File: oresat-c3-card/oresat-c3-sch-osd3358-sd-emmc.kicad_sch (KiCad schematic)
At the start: 48 parts, among them J5 DM3BT-DSF-PEJS, U1 OSD3358-1G-ISM, U8 TCAN330, U9 SFEM016GB1EA1TO-I-GE-121-STD

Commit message: All footprints updated. Passes ERC/DRC.
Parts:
- C16, C25: footprint Capacitor_SMD:C_0805_2012Metric -> oresat-passives:0805-C-NOSILK; DPN 490-GRT21BC71E106KE13LCT-ND -> 490-GRT21BC71E106KE13KCT-ND; DST Digi-Key -> DigiKey; MPN GRT21BC71E106KE13L -> GRT21BC71E106KE13K
- C17, C18: footprint Capacitor_SMD:C_0603_1608Metric -> oresat-passives:0603-C-NOSILK; DPN 587-3472-1-ND -> 399-6856-1-ND; MFR Taiyo Yuden -> KEMET; MPN TMK107BJ104KAHT -> C0603C104K5RACAUTO
- C19, C20, C21, C22, C23, C24: footprint Capacitor_SMD:C_0603_1608Metric -> oresat-passives:0603-C-NOSILK; DPN 587-3473-1-ND -> 490-GRT188R71E105KE13DCT-ND; MFR Taiyo Yuden -> Murata Electronics; MPN TMK107BJ105KAHT -> GRT188R71E105KE13D
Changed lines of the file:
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@@
 			)
 		)
-		(property "Footprint" "Capacitor_SMD:C_0603_1608Metric"
+		(property "Footprint" "oresat-passives:0603-C-NOSILK"
 			(at 360.68 149.86 0)
 			(effects
@@
 			)
 		)
-		(property "Datasheet" "~"
+		(property "Datasheet" "https://search.murata.co.jp/Ceramy/image/img/A01X/G101/ENG/GRT188R71E105KE13-01.pdf"
 			(at 360.68 149.86 0)
 			(effects
@@
 			)
 		)
-		(property "Description" "1µF ±10% 25V Ceramic Capacitor X5R 0603 (1608 Metric)"
+		(property "Description" "1 µF ±10% 25V Ceramic Capacitor X7R 0603 (1608 Metric)"
 			(at 360.68 149.86 0)
 			(effects
@@
 			)
 		)
-		(property "DPN" "587-3473-1-ND"
+		(property "DPN" "490-GRT188R71E105KE13DCT-ND"
 			(at 360.68 149.86 0)
 			(effects
@@
 			)
 		)
-		(property "MFR" "Taiyo Yuden"
+		(property "MFR" "Murata Electronics"
 			(at 360.68 149.86 0)
 			(effects
@@
 			)
 		)
-		(property "MPN" "TMK107BJ105KAHT"
+		(property "MPN" "GRT188R71E105KE13D"
 			(at 360.68 149.86 0)
 			(effects
@@
 			)
 		)
-		(property "Footprint" "Capacitor_SMD:C_0603_1608Metric"
+		(property "Footprint" "oresat-passives:0603-C-NOSILK"
 			(at 383.54 149.86 0)
 			(effects
@@
 			)
 		)
-		(property "Datasheet" "~"
+		(property "Datasheet" "https://search.murata.co.jp/Ceramy/image/img/A01X/G101/ENG/GRT188R71E105KE13-01.pdf"
 			(at 383.54 149.86 0)
 			(effects
@@
 			)
 		)
-		(property "Description" "1µF ±10% 25V Ceramic Capacitor X5R 0603 (1608 Metric)"
+		(property "Description" "1 µF ±10% 25V Ceramic Capacitor X7R 0603 (1608 Metric)"
 			(at 383.54 149.86 0)
 			(effects
@@
 			)
 		)
-		(property "DPN" "587-3473-1-ND"
+		(property "DPN" "490-GRT188R71E105KE13DCT-ND"
 			(at 383.54 149.86 0)
 			(effects
@@
 			)
 		)
-		(property "MFR" "Taiyo Yuden"
+		(property "MFR" "Murata Electronics"
 			(at 383.54 149.86 0)
 			(effects
@@
 			)
 		)
-		(property "MPN" "TMK107BJ105KAHT"
+		(property "MPN" "GRT188R71E105KE13D"
 			(at 383.54 149.86 0)
 			(effects
@@
 			)
 		)
-		(property "Footprint" "Capacitor_SMD:C_0805_2012Metric"
+		(property "Footprint" "oresat-passives:0805-C-NOSILK"
 			(at 57.15 110.49 0)
 			(effects
@@
 			)
 		)
-		(property "Datasheet" "~"
+		(property "Datasheet" "https://search.murata.co.jp/Ceramy/image/img/A01X/G101/ENG/GRT21BC71E106KE13-01.pdf"
 			(at 57.15 110.49 0)
 			(effects
@@
 			)
 		)
-		(property "DPN" "490-GRT21BC71E106KE13LCT-ND"
+		(property "DPN" "490-GRT21BC71E106KE13KCT-ND"
 			(at 57.15 110.49 0)
 			(effects
@@
 			)
 		)
-		(property "DST" "Digi-Key"
+		(property "DST" "DigiKey"
 			(at 57.15 110.49 0)
 			(effects
@@
 			)
 		)
-		(property "MPN" "GRT21BC71E106KE13L"
+		(property "MPN" "GRT21BC71E106KE13K"
 			(at 57.15 110.49 0)
 			(effects
@@
 			)
 		)
-		(property "Footprint" "Capacitor_SMD:C_0603_1608Metric"
+		(property "Footprint" "oresat-passives:0603-C-NOSILK"
 			(at 368.3 149.86 0)
 			(effects
@@
 			)
 		)
-		(property "Datasheet" "~"
+		(property "Datasheet" "https://search.murata.co.jp/Ceramy/image/img/A01X/G101/ENG/GRT188R71E105KE13-01.pdf"
 			(at 368.3 149.86 0)
 			(effects
@@
 			)
 		)
-		(property "Description" "1µF ±10% 25V Ceramic Capacitor X5R 0603 (1608 Metric)"
+		(property "Description" "1 µF ±10% 25V Ceramic Capacitor X7R 0603 (1608 Metric)"
 			(at 368.3 149.86 0)
 			(effects
@@
 			)
 		)
-		(property "DPN" "587-3473-1-ND"
+		(property "DPN" "490-GRT188R71E105KE13DCT-ND"
 			(at 368.3 149.86 0)
 			(effects
@@
 			)
 		)
-		(property "MFR" "Taiyo Yuden"
+		(property "MFR" "Murata Electronics"
 			(at 368.3 149.86 0)
 			(effects
@@
 			)
 		)
-		(property "MPN" "TMK107BJ105KAHT"
+		(property "MPN" "GRT188R71E105KE13D"
 			(at 368.3 149.86 0)
 			(effects
@@
 			)
 		)
-		(property "Footprint" "Capacitor_SMD:C_0603_1608Metric"
+		(property "Footprint" "oresat-passives:0603-C-NOSILK"
 			(at 345.44 149.86 0)
 			(effects
@@
 			)
 		)
-		(property "Datasheet" "~"
+		(property "Datasheet" "https://search.murata.co.jp/Ceramy/image/img/A01X/G101/ENG/GRT188R71E105KE13-01.pdf"
 			(at 345.44 149.86 0)
 			(effects
@@
 			)
 		)
-		(property "Description" "1µF ±10% 25V Ceramic Capacitor X5R 0603 (1608 Metric)"
+		(property "Description" "1 µF ±10% 25V Ceramic Capacitor X7R 0603 (1608 Metric)"
 			(at 345.44 149.86 0)
 			(effects
@@
 			)
 		)
-		(property "DPN" "587-3473-1-ND"
+		(property "DPN" "490-GRT188R71E105KE13DCT-ND"
 			(at 345.44 149.86 0)
 			(effects
@@
 			)
 		)
-		(property "MFR" "Taiyo Yuden"
+		(property "MFR" "Murata Electronics"
 			(at 345.44 149.86 0)
 			(effects
@@
 			)
 		)
-		(property "MPN" "TMK107BJ105KAHT"
+		(property "MPN" "GRT188R71E105KE13D"
 			(at 345.44 149.86 0)
 			(effects
@@
 			)
 		)
-		(property "Footprint" "Capacitor_SMD:C_0603_1608Metric"
+		(property "Footprint" "oresat-passives:0603-C-NOSILK"
 			(at 176.53 48.26 0)
 			(effects
@@
 			)
 		)
-		(property "Datasheet" "~"
+		(property "Datasheet" "https://search.kemet.com/download/specsheet/C0603C104K5RACAUTO"
 			(at 176.53 48.26 0)
 			(effects
@@
 			)
 		)
-		(property "Description" "100 nF (0.1µF) ±10% 25V Ceramic Capacitor X5R 0603 (1608 Metric)"
+		(property "Description" "0.1 µF ±10% 50V Ceramic Capacitor X7R 0603 (1608 Metric)"
 			(at 176.53 48.26 0)
 			(effects
@@
 			)
 		)
-		(property "DPN" "587-3472-1-ND"
+		(property "DPN" "399-6856-1-ND"
 			(at 176.53 48.26 0)
 			(effects
@@
 			)
 		)
-		(property "MFR" "Taiyo Yuden"
+		(property "MFR" "KEMET"
 			(at 176.53 48.26 0)
 			(effects
@@
 			)
 		)
-		(property "MPN" "TMK107BJ104KAHT"
+		(property "MPN" "C0603C104K5RACAUTO"
 			(at 176.53 48.26 0)
 			(effects
@@
 			)
 		)
-		(property "Footprint" "Capacitor_SMD:C_0603_1608Metric"
+		(property "Footprint" "oresat-passives:0603-C-NOSILK"
 			(at 375.92 149.86 0)
 			(effects
@@
 			)
 		)
-		(property "Datasheet" "~"
+		(property "Datasheet" "https://search.murata.co.jp/Ceramy/image/img/A01X/G101/ENG/GRT188R71E105KE13-01.pdf"
 			(at 375.92 149.86 0)
 			(effects
@@
 			)
 		)
-		(property "Description" "1µF ±10% 25V Ceramic Capacitor X5R 0603 (1608 Metric)"
+		(property "Description" "1 µF ±10% 25V Ceramic Capacitor X7R 0603 (1608 Metric)"
 			(at 375.92 149.86 0)
 			(effects
@@
 			)
 		)
-		(property "DPN" "587-3473-1-ND"
+		(property "DPN" "490-GRT188R71E105KE13DCT-ND"
 			(at 375.92 149.86 0)
 			(effects
@@
 			)
 		)
-		(property "MFR" "Taiyo Yuden"
+		(property "MFR" "Murata Electronics"
 			(at 375.92 149.86 0)
 			(effects
@@
 			)
 		)
-		(property "MPN" "TMK107BJ105KAHT"
+		(property "MPN" "GRT188R71E105KE13D"
 			(at 375.92 149.86 0)
 			(effects
@@
 			)
 		)
-		(property "Footprint" "Capacitor_SMD:C_0805_2012Metric"
+		(property "Footprint" "oresat-passives:0805-C-NOSILK"
 			(at 391.16 149.86 0)
 			(effects
@@
 			)
 		)
-		(property "Datasheet" "~"
+		(property "Datasheet" "https://search.murata.co.jp/Ceramy/image/img/A01X/G101/ENG/GRT21BC71E106KE13-01.pdf"
 			(at 391.16 149.86 0)
 			(effects
@@
 			)
 		)
-		(property "DPN" "490-GRT21BC71E106KE13LCT-ND"
+		(property "DPN" "490-GRT21BC71E106KE13KCT-ND"
 			(at 391.16 149.86 0)
 			(effects
@@
 			)
 		)
-		(property "DST" "Digi-Key"
+		(property "DST" "DigiKey"
 			(at 391.16 149.86 0)
 			(effects
@@
 			)
 		)
-		(property "MPN" "GRT21BC71E106KE13L"
+		(property "MPN" "GRT21BC71E106KE13K"
 			(at 391.16 149.86 0)
 			(effects
@@
 			)
 		)
-		(property "Footprint" "Capacitor_SMD:C_0603_1608Metric"
+		(property "Footprint" "oresat-passives:0603-C-NOSILK"
 			(at 355.6 149.86 0)
 			(effects
@@
 			)
 		)
-		(property "Datasheet" "~"
+		(property "Datasheet" "https://search.murata.co.jp/Ceramy/image/img/A01X/G101/ENG/GRT188R71E105KE13-01.pdf"
 			(at 355.6 149.86 0)
 			(effects
@@
 			)
 		)
-		(property "Description" "1µF ±10% 25V Ceramic Capacitor X5R 0603 (1608 Metric)"
+		(property "Description" "1 µF ±10% 25V Ceramic Capacitor X7R 0603 (1608 Metric)"
 			(at 355.6 149.86 0)
 			(effects
@@
 			)
 		)
-		(property "DPN" "587-3473-1-ND"
+		(property "DPN" "490-GRT188R71E105KE13DCT-ND"
 			(at 355.6 149.86 0)
 			(effects
@@
 			)
 		)
-		(property "MFR" "Taiyo Yuden"
+		(property "MFR" "Murata Electronics"
 			(at 355.6 149.86 0)
 			(effects
@@
 			)
 		)
-		(property "MPN" "TMK107BJ105KAHT"
+		(property "MPN" "GRT188R71E105KE13D"
 			(at 355.6 149.86 0)
 			(effects
@@
 			)
 		)
-		(property "Footprint" "Capacitor_SMD:C_0603_1608Metric"
+		(property "Footprint" "oresat-passives:0603-C-NOSILK"
 			(at 67.31 110.49 0)
 			(effects
@@
 			)
 		)
-		(property "Datasheet" "~"
+		(property "Datasheet" "https://search.kemet.com/download/specsheet/C0603C104K5RACAUTO"
 			(at 67.31 110.49 0)
 			(effects
@@
 			)
 		)
-		(property "Description" "100 nF (0.1µF) ±10% 25V Ceramic Capacitor X5R 0603 (1608 Metric)"
+		(property "Description" "0.1 µF ±10% 50V Ceramic Capacitor X7R 0603 (1608 Metric)"
 			(at 67.31 110.49 0)
 			(effects
@@
 			)
 		)
-		(property "DPN" "587-3472-1-ND"
+		(property "DPN" "399-6856-1-ND"
 			(at 67.31 110.49 0)
 			(effects
@@
 			)
 		)
-		(property "MFR" "Taiyo Yuden"
+		(property "MFR" "KEMET"
 			(at 67.31 110.49 0)
 			(effects
@@
 			)
 		)
-		(property "MPN" "TMK107BJ104KAHT"
+		(property "MPN" "C0603C104K5RACAUTO"
 			(at 67.31 110.49 0)
 			(effects

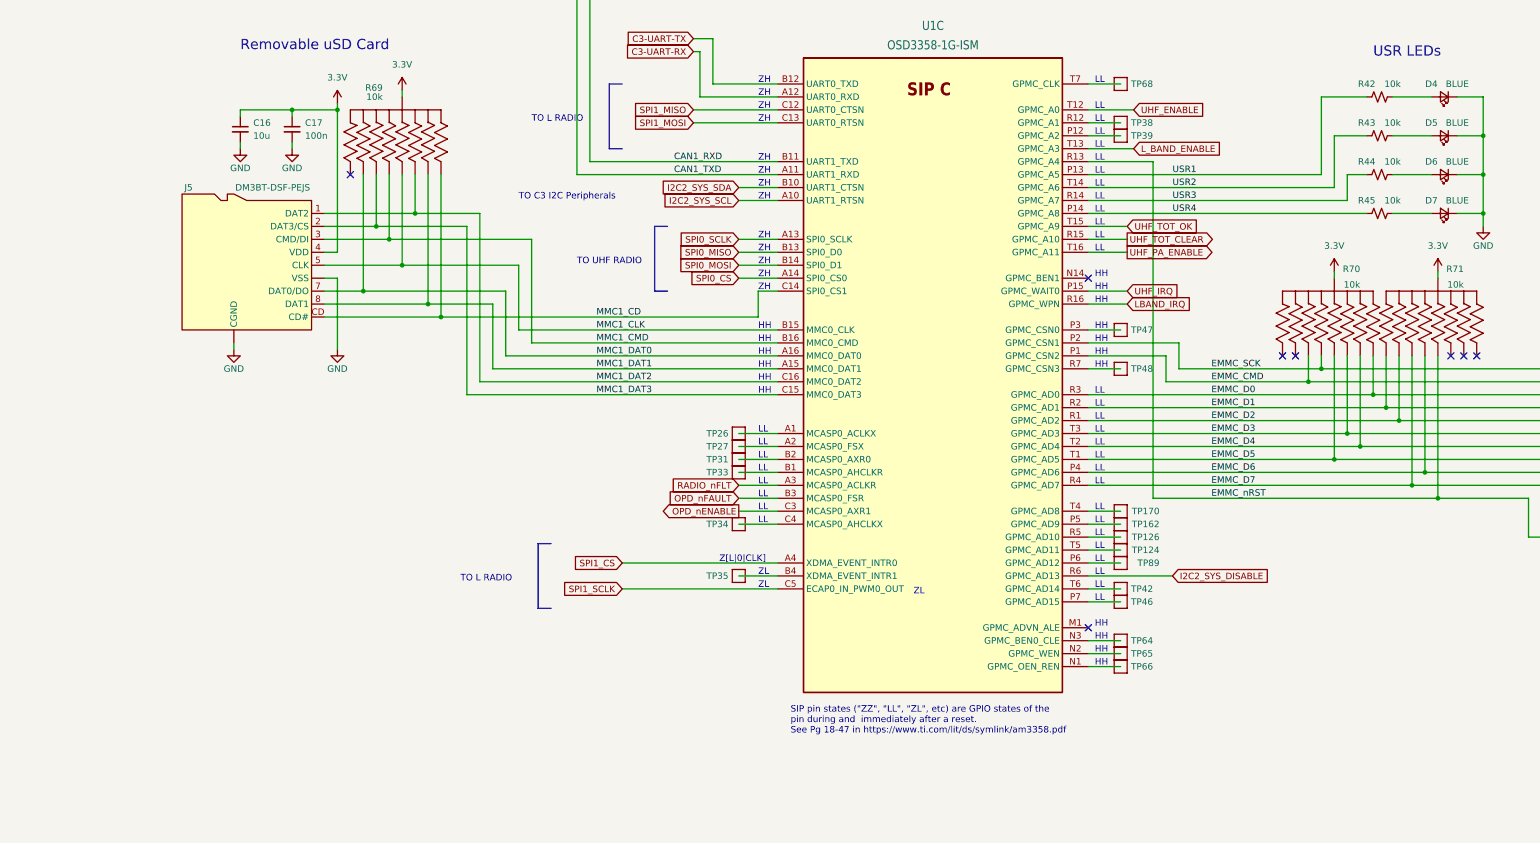
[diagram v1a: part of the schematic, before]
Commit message: All DRC exclusing RF traces are cleaned up.  RF traces cleaned up with mask and bends. Some more notes in the schematic for future us.
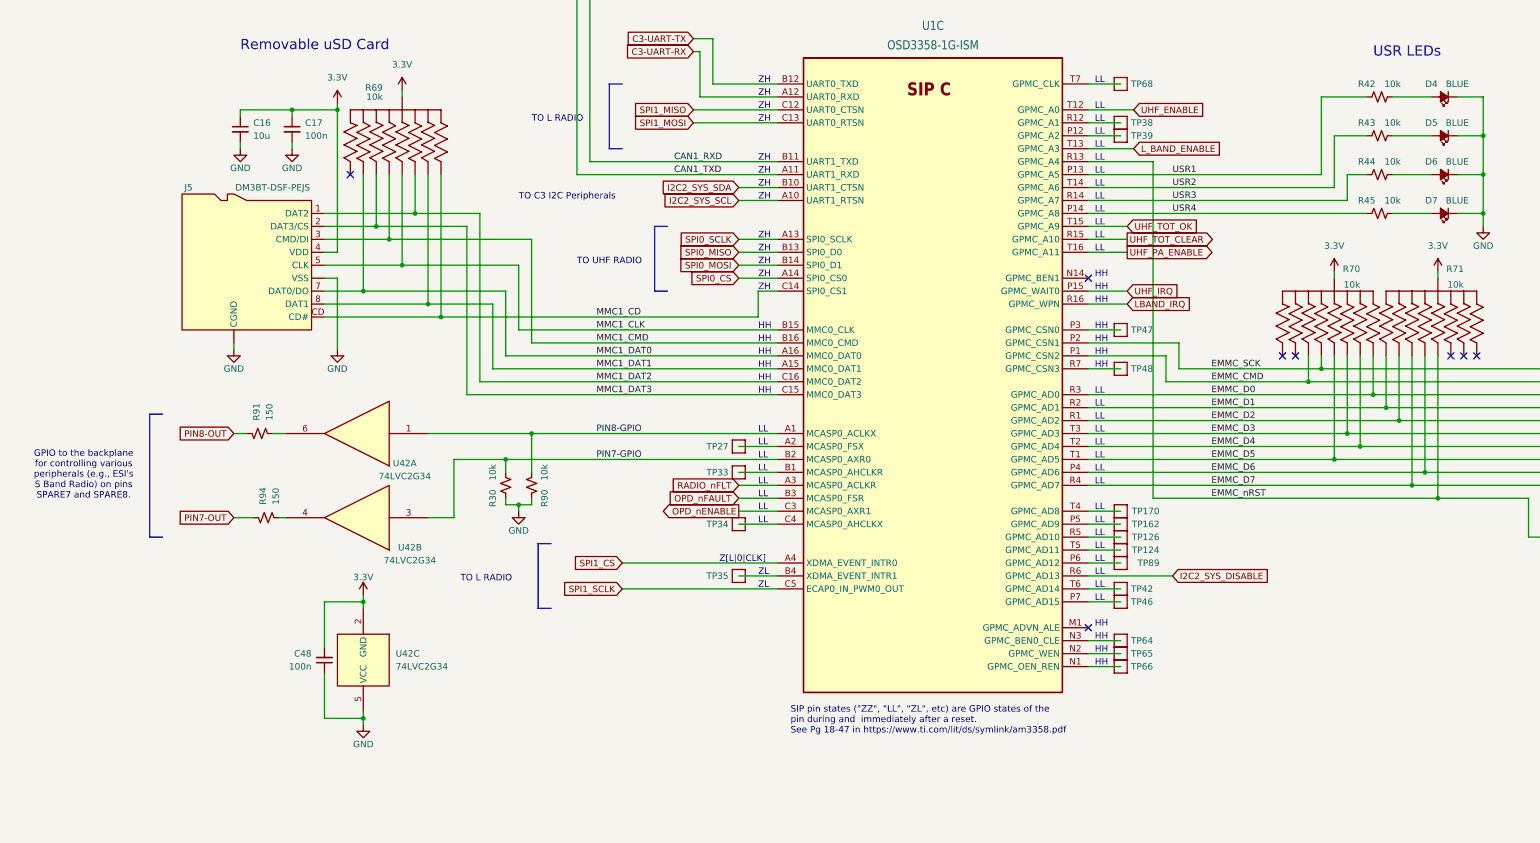
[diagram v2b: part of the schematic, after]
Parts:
- removed TP26, TP31: Test-Point, oresat-misc:TestPoint_Pad_D1.0mm, symbol oresat-misc:Test-Point-1mm-round
- added C48: 100n, oresat-passives:0603-C-NOSILK, symbol Device:C_Small
- added R30, R90: 10k, oresat-passives:0603-C-NOSILK, symbol Device:R_Small_US
- added R91, R94: 150, oresat-passives:0603-C-NOSILK, symbol Device:R_Small_US
- added U42: 74LVC2G34, Package_TO_SOT_SMD:SOT-363_SC-70-6, symbol 74xGxx:74LVC2G34
- D4, D5, D6, D7: symbol Device:LED_Small -> Device:LED_Small_Filled
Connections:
- net 3.3V: now also C48.2, U42.2 (GND)
- net GND: now also C48.1, R30.1, R90.1, U42.5 (VCC)
- net PIN7-GPIO: now reaches U1.B2 (MCASP0_AXR0)
- net PIN7-GPIO: now also R30.2, U42.3
- net PIN8-GPIO: now reaches U1.A1 (MCASP0_ACLKX)
- net PIN8-GPIO: now also R90.2, U42.1
- new net: R91.2, U42.6
- new net: R94.2, U42.4
- new net PIN7-OUT: R94.1
- new net PIN8-OUT: R91.1
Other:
- note added: "GPIO to the backplane for controlling various peripherals (e.g., ESI's S Band Radio) on pins SPARE7 and SPARE8."
